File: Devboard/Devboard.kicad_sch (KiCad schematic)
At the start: 36 parts, among them J1 USB_C_Receptacle_USB2.0_14P, J2 Conn_01x20, J3 Conn_01x20, J4 Conn_01x03, SW1 SW_Push, SW2 SW_Push, U1 RP2040, U2 MCP1700x-120xxMB, U3 W25Q128JVS, U4 ER_OLEDM0.91_1x-I2C, Y2 Crystal_GND24

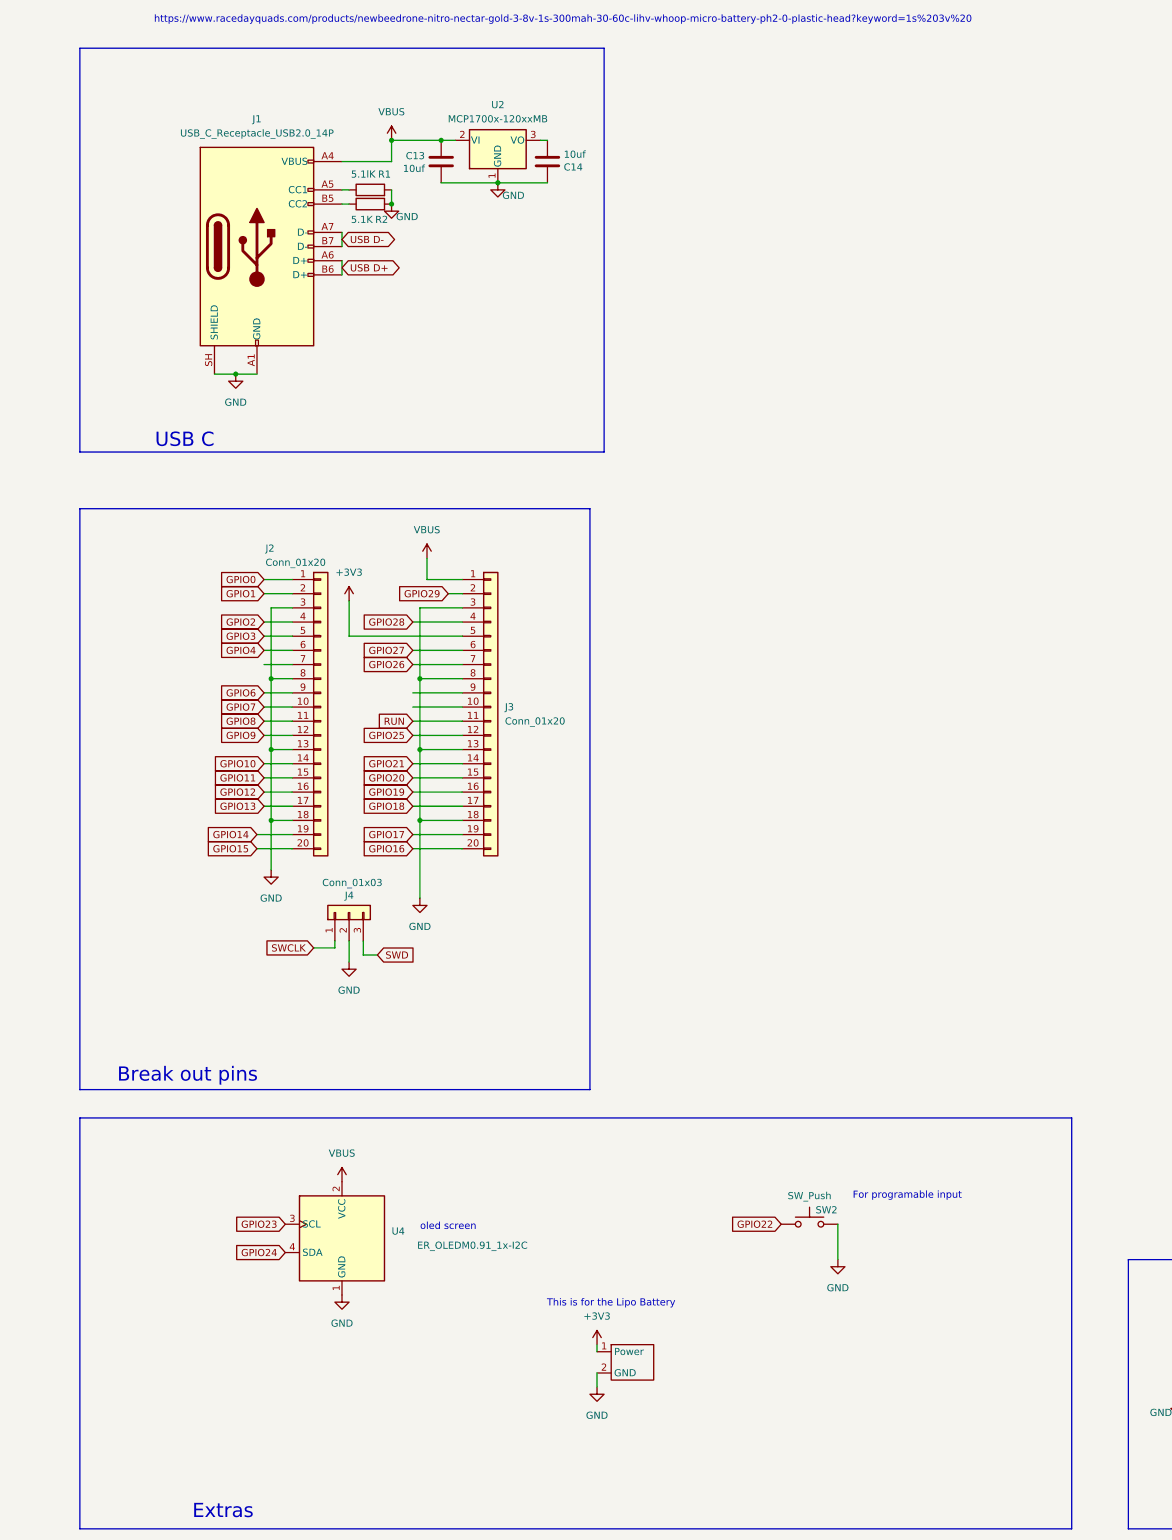
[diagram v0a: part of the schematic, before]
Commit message: Added the TPS63000 buck-boost converter
Next, I need to route everything again. I also need to finish the BOM. The silkscreen could also use some work imo. I also had to change some of the symbols. I will likely be doing pcba.

https://lapse.hackclub.com/timelapse/hDr_HyoGHTTv

https://lapse.hackclub.com/timelapse/UjBjIMcLNt3x
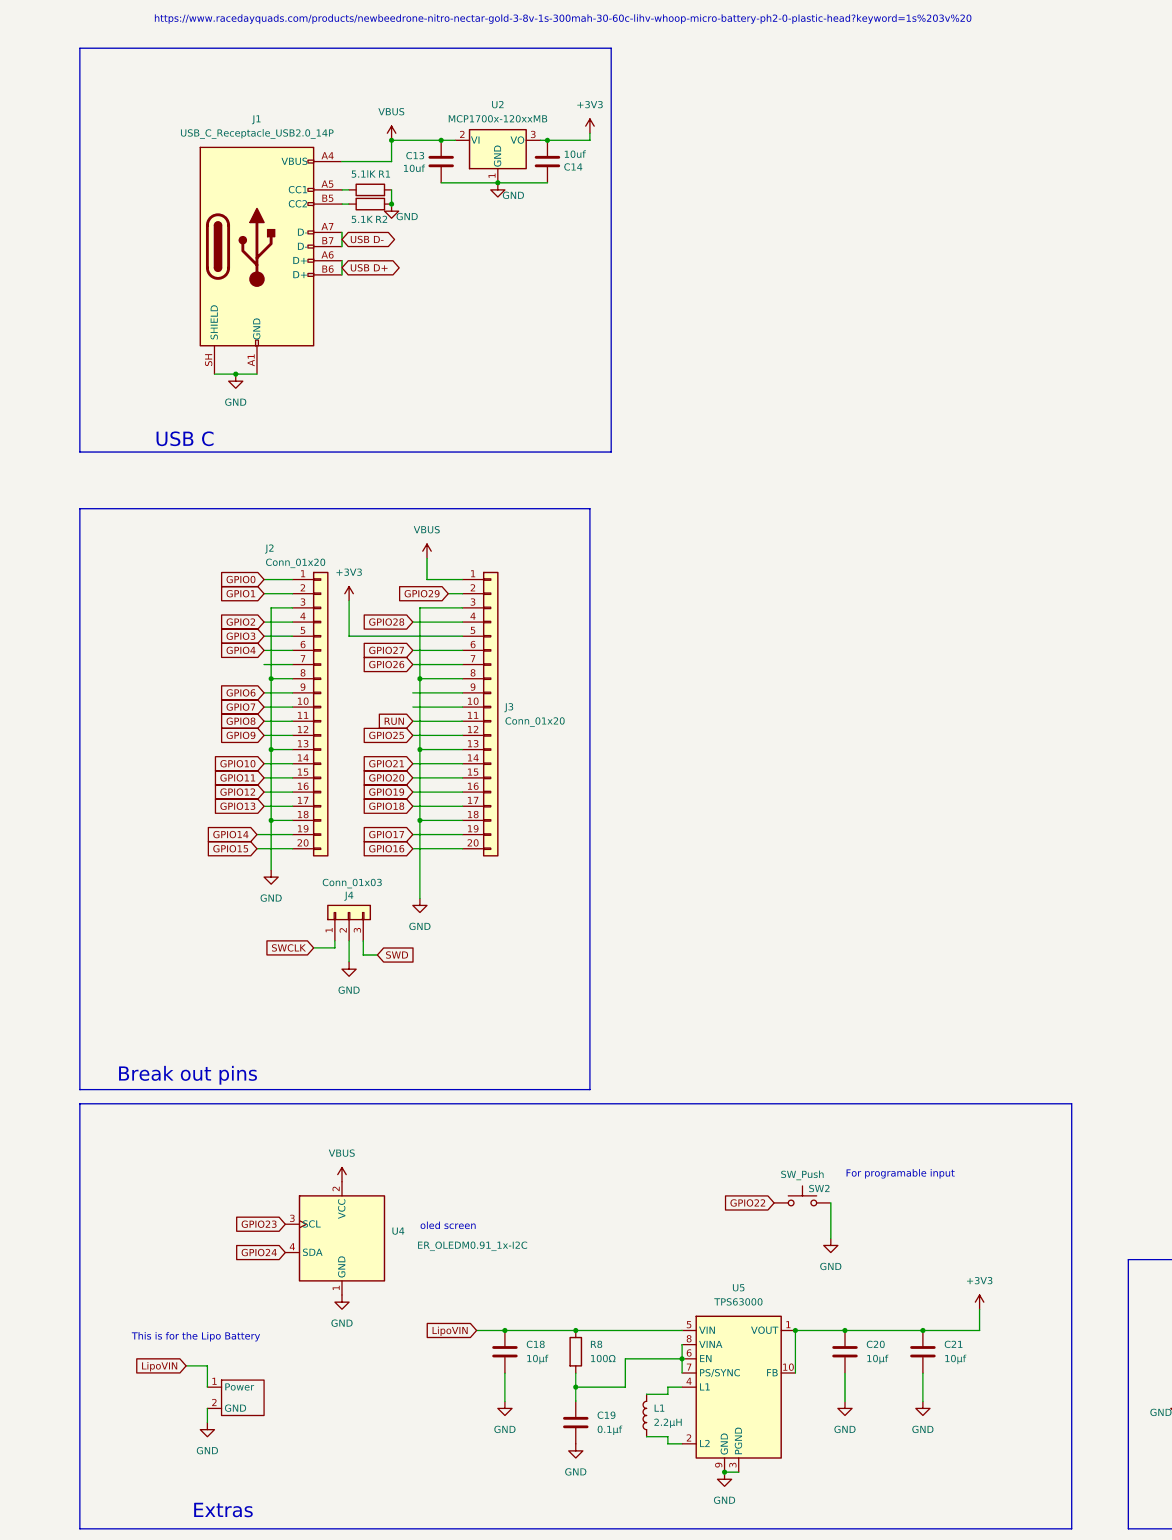
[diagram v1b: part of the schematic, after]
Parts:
- added C18, C20, C21: 10μf, Capacitor_SMD:C_0201_0603Metric, symbol Device:C
- added C19: 0.1μf, Capacitor_SMD:C_0201_0603Metric, symbol Device:C
- added L1: 2.2μH, Inductor_SMD:L_6.3x6.3_H3, symbol Device:L
- added R8: 100Ω, Resistor_SMD:R_0201_0603Metric, symbol Device:R
- added U5: TPS63000, Package_SON:Texas_DRC0010J_ThermalVias, symbol Regulator_Switching:TPS63000
- C1, C10, C11, C12, C13, C14, C15, C16, C17, C2, C3, C4, C5, C6, C7, C8, C9: footprint Capacitor_SMD:C_0201_0603Metric_Pad0.64x0.40mm_HandSolder -> Capacitor_SMD:C_0201_0603Metric
- R1, R2, R3, R4, R5, R6, R7: footprint Resistor_SMD:R_0402_1005Metric_Pad0.72x0.64mm_HandSolder -> Resistor_SMD:R_0402_1005Metric
- Y2: footprint Crystal:Crystal_SMD_3225-4Pin_3.2x2.5mm_HandSoldering -> Crystal:Crystal_SMD_3225-4Pin_3.2x2.5mm
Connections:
- net +3V3: now also C14.2, U2.3 (VO), C20.1, C21.1, U5.1 (VOUT), U5.10 (FB); no longer XT1.1 (Power)
- net GND: now also C18.2, C19.2, C20.2, C21.2, U5.11 (PGND), U5.3 (PGND), U5.9 (GND)
- new net: C19.1, R8.2, U5.6 (EN), U5.7 (PS/SYNC), U5.8 (VINA)
- new net: L1.1, U5.2 (L2)
- new net: L1.2, U5.4 (L1)
- new net LipoVIN: C18.1, R8.1, U5.5 (VIN), XT1.1 (Power)
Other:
- moved on the sheet: SW2

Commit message: Journaled and worked on getting a render done.
I got a basic render working with the silkscreen. Orignally I had trouble trying to make the silscreen show up. The solution was to raise the silkscreen above the rest of the pcb 3d model.
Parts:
- R1: value 5.1lK -> 5.1KΩ
- R2: value 5.1K -> 5.1KΩ
- R3, R4: value 27 -> 27Ω
- R6: value 1K -> 1KΩ
- R7: value 10K -> 10KΩ
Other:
- note added: "Flash memory"
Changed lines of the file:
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@@
 		)
 	)
+	(text "Flash memory"
+		(exclude_from_sim no)
+		(at 346.964 76.454 0)
+		(effects
+			(font
+				(size 2.54 2.54)
+			)
+		)
+	)
 	(text "USB C"
 		(exclude_from_sim no)
@@
 	(text "RP2040 and Decoupling Caps"
 		(exclude_from_sim no)
-		(at 343.662 76.454 0)
+		(at 342.9 84.328 0)
 		(effects
 			(font
@@
 	(wire
 		(pts
-			(xy 118.11 267.97) (xy 118.11 269.24)
-		)
-		(stroke
-			(width 0)
-			(type default)
-		)
-	)
-	(wire
-		(pts
 			(xy 110.49 259.08) (xy 101.6 259.08)
 		)
@@
 	(wire
 		(pts
-			(xy 114.3 260.35) (xy 118.11 260.35)
-		)
-		(stroke
-			(width 0)
-			(type default)
-		)
-	)
-	(wire
-		(pts
 			(xy 59.69 57.15) (xy 59.69 59.69)
 		)
@@
 	(wire
 		(pts
-			(xy 114.3 267.97) (xy 118.11 267.97)
-		)
-		(stroke
-			(width 0)
-			(type default)
-		)
-	)
-	(wire
-		(pts
 			(xy 77.47 35.56) (xy 80.01 35.56)
 		)
@@
 	(wire
 		(pts
-			(xy 118.11 269.24) (xy 120.65 269.24)
-		)
-		(stroke
-			(width 0)
-			(type default)
-		)
-	)
-	(wire
-		(pts
 			(xy 260.35 92.71) (xy 271.78 92.71)
 		)
@@
 	(wire
 		(pts
-			(xy 118.11 259.08) (xy 120.65 259.08)
-		)
-		(stroke
-			(width 0)
-			(type default)
-		)
-	)
-	(wire
-		(pts
 			(xy 73.66 157.48) (xy 81.28 157.48)
 		)
@@
 	(wire
 		(pts
+			(xy 114.3 259.08) (xy 120.65 259.08)
+		)
+		(stroke
+			(width 0)
+			(type default)
+		)
+	)
+	(wire
+		(pts
 			(xy 140.97 248.92) (xy 140.97 256.54)
 		)
@@
 	(wire
 		(pts
+			(xy 114.3 267.97) (xy 114.3 269.24)
+		)
+		(stroke
+			(width 0)
+			(type default)
+		)
+	)
+	(wire
+		(pts
 			(xy 163.83 256.54) (xy 163.83 261.62)
 		)
@@
 	(wire
 		(pts
+			(xy 114.3 269.24) (xy 120.65 269.24)
+		)
+		(stroke
+			(width 0)
+			(type default)
+		)
+	)
+	(wire
+		(pts
 			(xy 140.97 248.92) (xy 149.86 248.92)
 		)
@@
 	(wire
 		(pts
+			(xy 114.3 260.35) (xy 114.3 259.08)
+		)
+		(stroke
+			(width 0)
+			(type default)
+		)
+	)
+	(wire
+		(pts
 			(xy 295.91 92.71) (xy 306.07 92.71)
 		)
@@
 	(wire
 		(pts
-			(xy 118.11 260.35) (xy 118.11 259.08)
-		)
-		(stroke
-			(width 0)
-			(type default)
-		)
-	)
-	(wire
-		(pts
 			(xy 350.52 41.91) (xy 353.06 41.91)
 		)
@@
 		(dnp no)
 		(property "Reference" "R3"
-			(at 355.092 152.146 90)
+			(at 356.108 152.146 90)
 			(show_name no)
 			(do_not_autoplace no)
@@
 			)
 		)
-		(property "Value" "27"
+		(property "Value" "27Ω"
 			(at 351.536 152.146 90)
 			(show_name no)
@@
 			)
 		)
-		(property "Value" "1K"
+		(property "Value" "1KΩ"
 			(at 346.71 38.1 90)
 			(show_name no)
@@
 			)
 		)
-		(property "Value" "5.1K"
-			(at 63.246 49.784 90)
+		(property "Value" "5.1KΩ"
+			(at 61.722 49.784 90)
 			(show_name no)
 			(do_not_autoplace no)
@@
 			)
 		)
-		(property "Value" "5.1lK"
-			(at 63.5 41.656 90)
+		(property "Value" "5.1KΩ"
+			(at 62.484 41.656 90)
 			(show_name no)
 			(do_not_autoplace no)
@@
 			)
 		)
-		(property "Value" "10K"
+		(property "Value" "10KΩ"
 			(at 355.092 39.624 0)
 			(show_name no)
@@
 		(dnp no)
 		(property "Reference" "R4"
-			(at 354.33 160.02 90)
+			(at 355.6 160.02 90)
 			(show_name no)
 			(do_not_autoplace no)
@@
 			)
 		)
-		(property "Value" "27"
+		(property "Value" "27Ω"
 			(at 351.282 160.02 90)
 			(show_name no)
